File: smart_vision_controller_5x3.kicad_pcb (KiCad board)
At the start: 2 copper layers, 121.3 x 67.3 mm, 1 part

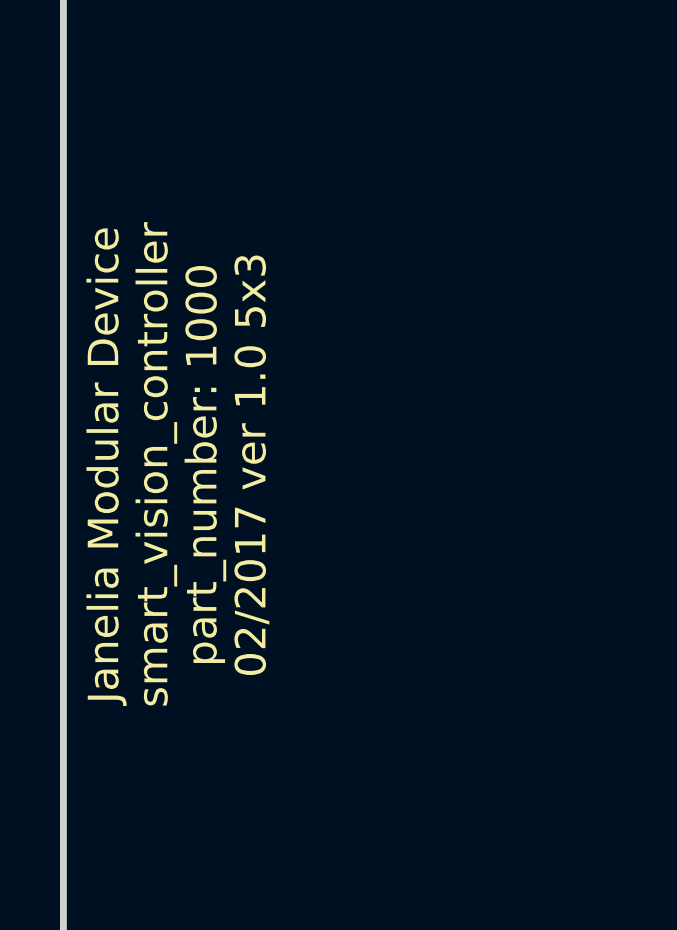
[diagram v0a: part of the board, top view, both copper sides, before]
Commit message: Added some components and footprints.
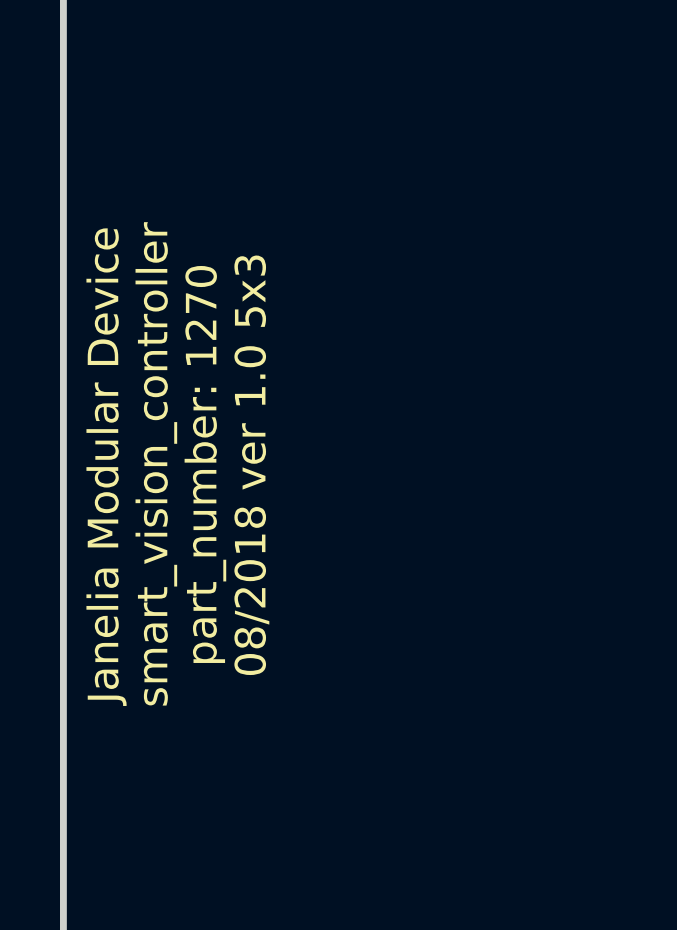
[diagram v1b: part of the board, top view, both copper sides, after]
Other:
- board text added: "Janelia Modular Device smart_vision_controller part_number: 1270 08/2018 ver 1.0 5x3"
- board text removed: "Janelia Modular Device smart_vision_controller part_number: 1000 02/2017 ver 1.0 5x3"
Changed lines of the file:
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@@
-(kicad_pcb (version 20170123) (host pcbnew no-vcs-found-0633d90~59~ubuntu16.04.1)
+(kicad_pcb (version 20171130) (host pcbnew 6.0.0-rc1-unknown-3eb3db0~66~ubuntu18.04.1)
   (general
     (thickness 1.6)
@@
     (zone_45_only no)
     (trace_min 0.254)
-    (segment_width 0.2286)
-    (edge_width 0.2286)
     (via_size 0.889)
     (via_drill 0.635)
@@
     (uvia_min_size 0.508)
     (uvia_min_drill 0.127)
+    (edge_width 0.2286)
+    (segment_width 0.2286)
     (pcb_text_width 0.3)
     (pcb_text_size 1.5 1.5)
@@
       (layerselection 0x000f0_ffffffff)
       (usegerberextensions true)
+      (usegerberattributes false)
+      (usegerberadvancedattributes false)
+      (creategerberjobfile false)
       (excludeedgelayer false)
       (linewidth 0.100000)
@@
       (hpglpennumber 1)
       (hpglpenspeed 20)
-      (hpglpendiameter 15)
+      (hpglpendiameter 15.000000)
       (psnegative false)
       (psa4output false)
@@
       (drillshape 0)
       (scaleselection 1)
-      (outputdirectory gerbers/))
+      (outputdirectory "gerbers/"))
   )
   (net 0 "")
@@
     (uvia_dia 0.508)
     (uvia_drill 0.127)
-    (diff_pair_gap 0.254)
-    (diff_pair_width 0.254)
+    (diff_pair_width 0.254)
+    (diff_pair_gap 0.254)
   )
   (net_class GND ""
@@
     (uvia_dia 0.508)
     (uvia_drill 0.127)
-    (diff_pair_gap 0.254)
-    (diff_pair_width 0.254)
+    (diff_pair_width 0.254)
+    (diff_pair_gap 0.254)
   )
   (net_class LEDPOWER ""
@@
     (uvia_dia 0.508)
     (uvia_drill 0.127)
-    (diff_pair_gap 0.254)
-    (diff_pair_width 0.254)
+    (diff_pair_width 0.254)
+    (diff_pair_gap 0.254)
   )
   (net_class POWER ""
@@
     (uvia_dia 0.508)
     (uvia_drill 0.127)
-    (diff_pair_gap 0.254)
-    (diff_pair_width 0.254)
+    (diff_pair_width 0.254)
+    (diff_pair_gap 0.254)
   )
   (net_class SIGNAL ""
@@
     (uvia_dia 0.508)
     (uvia_drill 0.127)
-    (diff_pair_gap 0.254)
-    (diff_pair_width 0.254)
+    (diff_pair_width 0.254)
+    (diff_pair_gap 0.254)
   )
   (net_class SUPERPOWER ""
@@
     (uvia_dia 0.508)
     (uvia_drill 0.127)
-    (diff_pair_gap 0.254)
-    (diff_pair_width 0.254)
+    (diff_pair_width 0.254)
+    (diff_pair_gap 0.254)
   )
   (module smart_vision_controller_5x3:MODULAR_DEVICE_BASE_5X3_MALE (layer F.Cu)
@@
     )
     (fp_text value MODULAR_DEVICE_BASE_5x3_MALE (at 0 2.54) (layer F.SilkS) hide
-      (effects (font (thickness 0.3048)))
+      (effects (font (size 1.524 1.524) (thickness 0.3048)))
     )
     (fp_circle (center 73.66 30.48) (end 76.2 30.48) (layer F.SilkS) (width 0.2286))
@@
     (effects (font (size 1.016 1.016) (thickness 0.1905)))
   )
-  (gr_text "Janelia Modular Device\nsmart_vision_controller\npart_number: 1000\n02/2017 ver 1.0 5x3" (at 73.66 105.41 90) (layer F.SilkS)
+  (gr_text "Janelia Modular Device\nsmart_vision_controller\npart_number: 1270\n08/2018 ver 1.0 5x3" (at 73.66 105.41 90) (layer F.SilkS)
     (effects (font (size 1.016 1.016) (thickness 0.254)))
   )

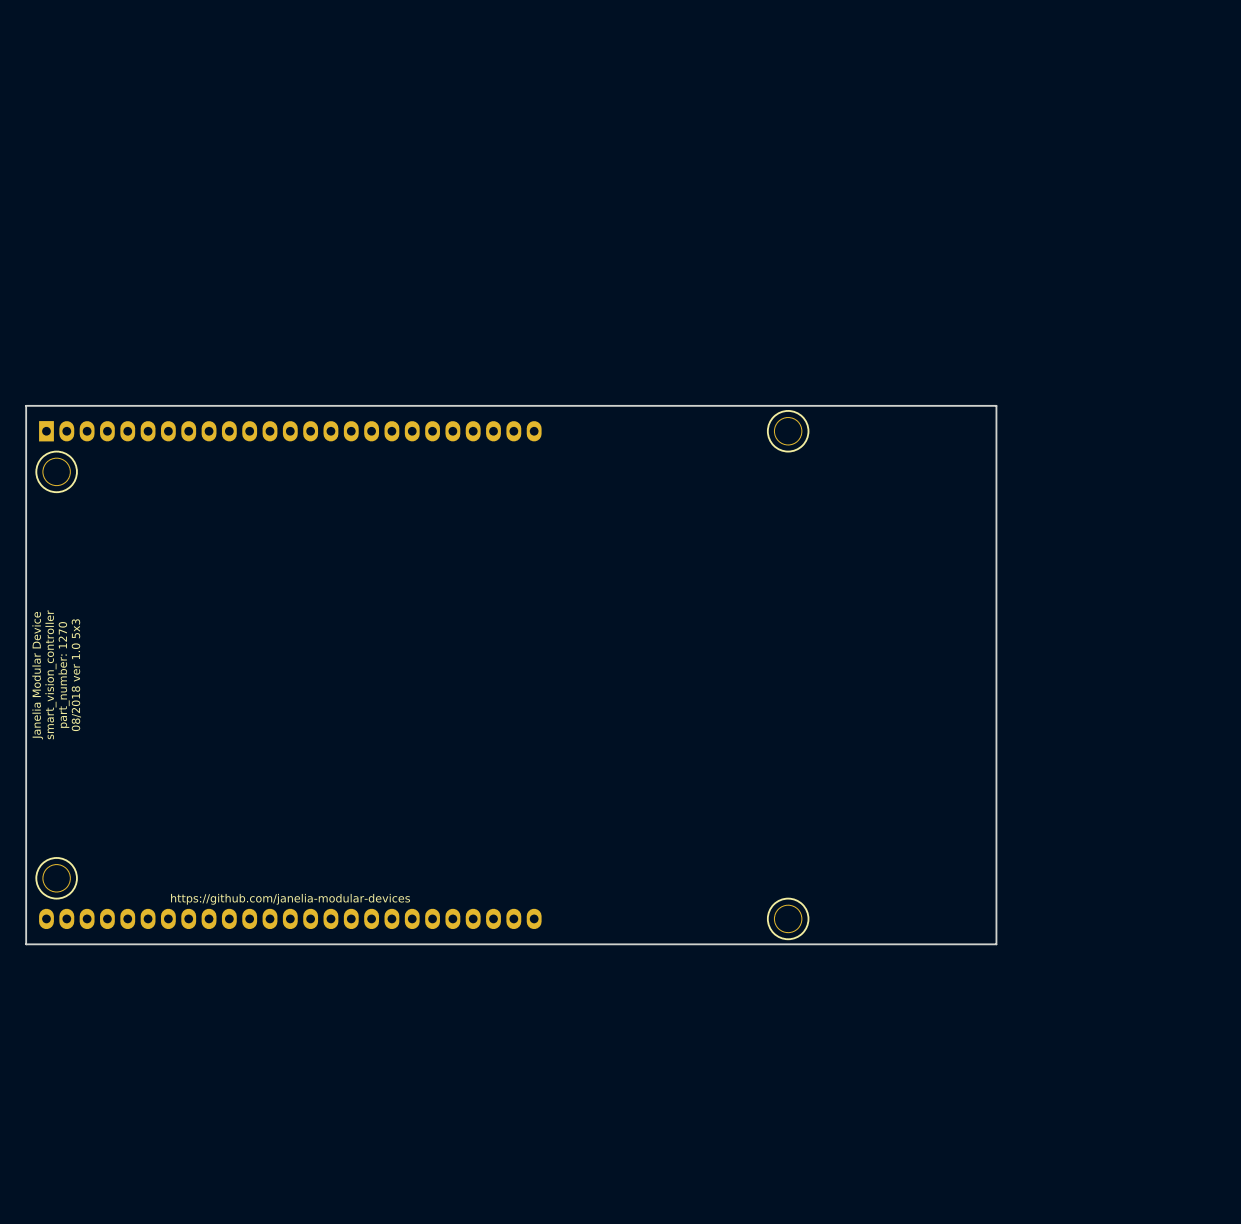
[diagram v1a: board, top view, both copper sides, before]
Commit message: Removed F.SilkS from pads.
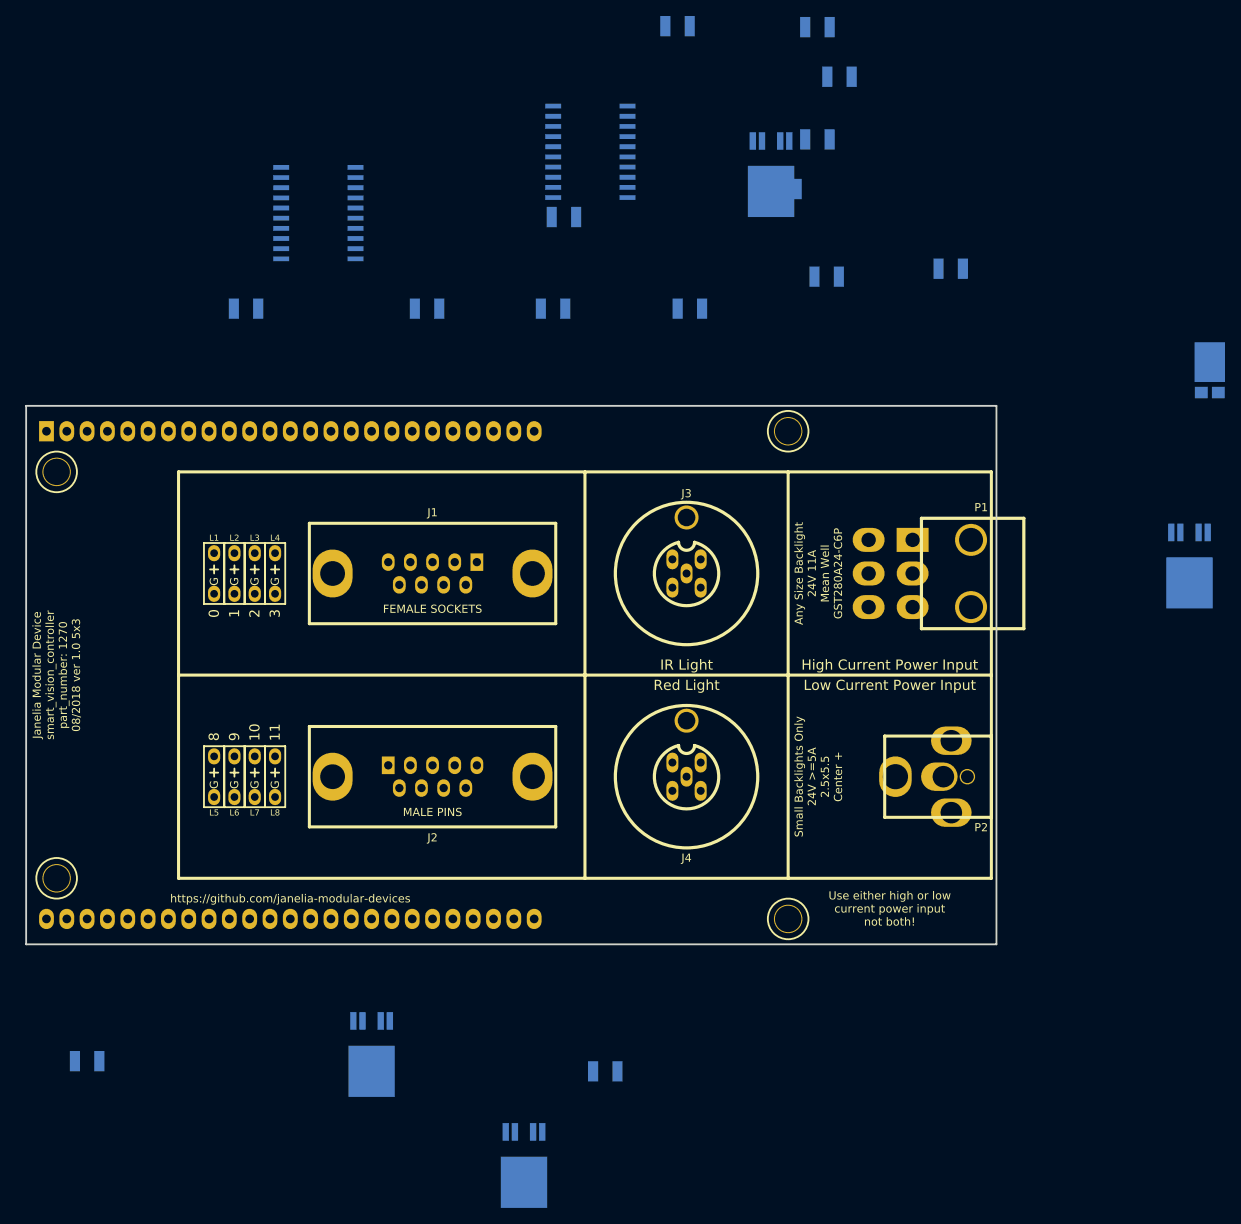
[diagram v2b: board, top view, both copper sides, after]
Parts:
- added C1: 0.1uF, smart_vision_controller_5x3:SM1210, B.Cu at (151.3, 24.3)
- added C2: 0.1uF, smart_vision_controller_5x3:SM1210, B.Cu at (137.1, 48.2)
- added C3: 0.1uF, smart_vision_controller_5x3:SM1210, B.Cu at (97.3, 59.6)
- added C4: 0.1uF, smart_vision_controller_5x3:SM1210, B.Cu at (185.4, 54.6)
- added C5: 0.1uF, smart_vision_controller_5x3:SM1210, B.Cu at (120.0, 59.6)
- added C6: 0.1uF, smart_vision_controller_5x3:SM1210, B.Cu at (168.8, 38.5)
- added D1: diode_schottky_45V_10A, smart_vision_controller_5x3:CFP15, B.Cu at (217.8, 67.3)
- added HPS1: BTS3256, smart_vision_controller_5x3:PG-TO252-5-11, B.Cu at (113.0, 148.6)
- added HPS2: BTS3256, smart_vision_controller_5x3:PG-TO252-5-11, B.Cu at (215.3, 87.6)
- added HPS3: BTS3256, smart_vision_controller_5x3:PG-TO252-5-11, B.Cu at (132.1, 162.5)
- added HPS4: BTS3256, smart_vision_controller_5x3:PG-TO252-5-11, B.Cu at (163.0, 38.7)
- added J1: DB9F, smart_vision_controller_5x3:DB9F, F.Cu at (120.7, 92.7)
- added J2: DB9M, smart_vision_controller_5x3:DB9M, F.Cu at (120.7, 118.1)
- added J3: M12-5_RCPT_F, smart_vision_controller_5x3:M12-5_RCPT_F, F.Cu at (152.4, 92.7)
- added J4: M12-5_RCPT_F, smart_vision_controller_5x3:M12-5_RCPT_F, F.Cu at (152.4, 118.1)
- added L1: LED_5V_GRN, smart_vision_controller_5x3:LED_555-3XXX_G, F.Cu at (93.3, 92.7)
- added L2: LED_5V_GRN, smart_vision_controller_5x3:LED_555-3XXX_G, F.Cu at (95.9, 92.7)
- added L3: LED_5V_GRN, smart_vision_controller_5x3:LED_555-3XXX_G, F.Cu at (98.4, 92.7)
- added L4: LED_5V_GRN, smart_vision_controller_5x3:LED_555-3XXX_G, F.Cu at (101.0, 92.7)
- added L5: LED_5V_GRN, smart_vision_controller_5x3:LED_555-3XXX_G, F.Cu at (93.3, 118.1)
- added L6: LED_5V_GRN, smart_vision_controller_5x3:LED_555-3XXX_G, F.Cu at (95.9, 118.1)
- added L7: LED_5V_GRN, smart_vision_controller_5x3:LED_555-3XXX_G, F.Cu at (98.4, 118.1)
- added L8: LED_5V_GRN, smart_vision_controller_5x3:LED_555-3XXX_G, F.Cu at (101.0, 118.1)
- added P1: MINI_FIT_JR_02X03_M_RA, smart_vision_controller_5x3:MINI-FIT-JR_02X03_M_RA, F.Cu at (188.0, 92.7)
- added P2: PWR_JACK_2.5x5.5, smart_vision_controller_5x3:DCJACK_2PIN_HIGHCURRENT, F.Cu at (190.5, 118.1)
- added R1: 5.9k, smart_vision_controller_5x3:SM1210, B.Cu at (77.5, 153.7)
- added R2: 5.9k, smart_vision_controller_5x3:SM1210, B.Cu at (168.8, 24.4)
- added R3: 5.9k, smart_vision_controller_5x3:SM1210, B.Cu at (142.2, 154.9)
- added R4: 5.9k, smart_vision_controller_5x3:SM1210, B.Cu at (171.5, 30.6)
- added R5: 35.7, smart_vision_controller_5x3:SM1210, B.Cu at (135.7, 59.6)
- added R6: 35.7, smart_vision_controller_5x3:SM1210, B.Cu at (164.6, 44.7)
- added R7: 35.7, smart_vision_controller_5x3:SM1210, B.Cu at (152.8, 59.6)
- added R8: 35.7, smart_vision_controller_5x3:SM1210, B.Cu at (169.9, 55.6)
- added U1: SN74ABT541BDWR, smart_vision_controller_5x3:SOIC_20, B.Cu at (140.4, 40.0)
- added U2: SN74ABT541BDWR, smart_vision_controller_5x3:SOIC_20, B.Cu at (106.4, 47.7)
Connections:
- MDB1 pad 14: (no net) -> /SIGNAL_8
- MDB1 pad 15: (no net) -> /SIGNAL_9
- MDB1 pad 16: (no net) -> /SIGNAL_10
- MDB1 pad 17: (no net) -> /SIGNAL_11
- MDB1 pad 18: (no net) -> /SIGNAL_12
- MDB1 pad 19: (no net) -> /SIGNAL_13
- MDB1 pad 2: (no net) -> /SIGNAL_0
- MDB1 pad 20: (no net) -> /SIGNAL_14
- MDB1 pad 21: (no net) -> /SIGNAL_15
- MDB1 pad 22: (no net) -> /SIGNAL_6
- MDB1 pad 23: (no net) -> /SIGNAL_7
- MDB1 pad 29: (no net) -> /SIGNAL_2
- MDB1 pad 30: (no net) -> /SIGNAL_3
- MDB1 pad 35: (no net) -> /SIGNAL_4
- MDB1 pad 36: (no net) -> /SIGNAL_5
- MDB1 pad 52: (no net) -> /~ENABLE
- MDB1 pad 6: (no net) -> /SIGNAL_1
- MDB1 pad GND: (no net) -> GND
- MDB1 pad VDD: (no net) -> VDD
- MDB1 pad VEE: (no net) -> VEE
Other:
- board text added: "0"
- board text added: "1"
- board text added: "10"
- board text added: "11"
- board text added: "2"
- board text added: "3"
- board text added: "8"
- board text added: "9"
- board text added: "Any Size Backlight 24V 11A Mean Well GST280A24-C6P"
- board text added: "High Current Power Input"
- board text added: "IR Light"
- board text added: "Low Current Power Input"
- board text added: "Red Light"
- board text added: "Small Backlights Only 24V >=5A 2.5x5.5 Center +"
- board text added: "Use either high or low current power input not both!"

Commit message: Finished layout of v1.0.
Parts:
- moved D1 136.4 mm to (81.9, 79.4), turned to 90 degrees
- moved R4 136.0 mm to (73.0, 124.5), turned to 180 degrees
- moved HPS2 135.1 mm to (80.6, 99.1), turned to 90 degrees
- moved C6 125.4 mm to (77.5, 124.5), turned to 90 degrees
- moved R2 121.4 mm to (73.0, 99.1), turned to 180 degrees
- moved HPS4 118.9 mm to (80.6, 124.5), turned to 90 degrees
- moved C4 116.7 mm to (77.5, 99.1), turned to 90 degrees
- moved C1 97.7 mm to (111.8, 113.7)
- moved R3 81.6 mm to (73.0, 111.8), turned to 180 degrees
- moved HPS3 72.3 mm to (80.6, 111.8), turned to 90 degrees
- moved U1 71.4 mm to (111.8, 105.4), turned to 180 degrees
- moved HPS1 70.2 mm to (80.6, 86.4), turned to 90 degrees
- moved U2 68.7 mm to (143.5, 105.4), turned to 180 degrees
- moved R1 68.1 mm to (73.0, 85.7), turned to 180 degrees
- moved C5 67.3 mm to (77.5, 111.8), turned to 90 degrees
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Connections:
- net /RED renamed /VISIBLE
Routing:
- net GND: track 0.00 -> 337.9 mm, vias 0 -> 1
- net VAA: track 0.00 -> 197.3 mm, vias 0 -> 1
- net VEE: track 0.00 -> 111.2 mm, vias 0 -> 2
- net /~ENABLE: track 0.00 -> 95.5 mm
- net /SIGNAL_13: track 0.00 -> 91.6 mm
- net /SIGNAL_12: track 0.00 -> 90.6 mm
- net /SIGNAL_11: track 0.00 -> 90.6 mm
- net /SIGNAL_9: track 0.00 -> 85.7 mm, vias 0 -> 1
- net VDD: track 0.00 -> 82.1 mm
- net /S_3: track 0.00 -> 79.8 mm
- net /SIGNAL_15: track 0.00 -> 77.5 mm, vias 0 -> 1
- net /SIGNAL_5: track 0.00 -> 71.0 mm, vias 0 -> 1
- net /SIGNAL_14: track 0.00 -> 70.5 mm, vias 0 -> 1
- net /SIGNAL_10: track 0.00 -> 65.5 mm, vias 0 -> 1
- net /SIGNAL_8: track 0.00 -> 63.2 mm, vias 0 -> 1
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- added copper zone on B.Cu, net GND
- added copper zone on F.Cu, net VAA
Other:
- net class POWER: trace_width 0.8128 -> 1.2192; via_dia 0.889 -> 1.2192; via_drill 0.635 -> 0.7112
- net class SUPERPOWER: trace_width 1.2192 -> 1.6256; via_dia 0.889 -> 1.6256; via_drill 0.635 -> 1.1176
- board text added: "24V Output Channels"
- board text added: "5V Output Channels"
- board text added: "Visible Light"
- board text removed: "Red Light"
